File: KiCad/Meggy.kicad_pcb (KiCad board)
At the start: 4 copper layers, 17.4 x 54 mm, 24 parts, among them J1 USB_B_Micro, J2 Conn_01x03, Q1 DMP2305U-7, Q2 DMP2305U-7, Q3 DMP2305U-7, U1 ROM-socket-42pin, U2 AT90USB1286-MU, U3 M29F160F, X1 Standard_Clock_Oscillators_XT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

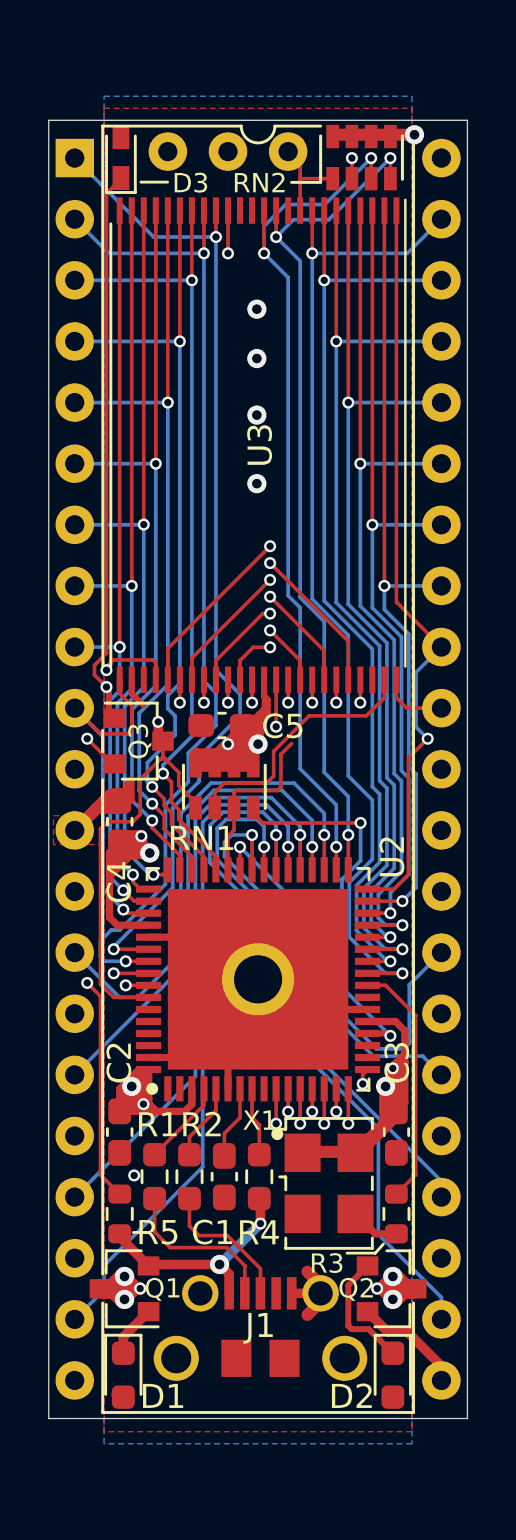
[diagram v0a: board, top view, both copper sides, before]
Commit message: Add push button for RESET and HWB lines
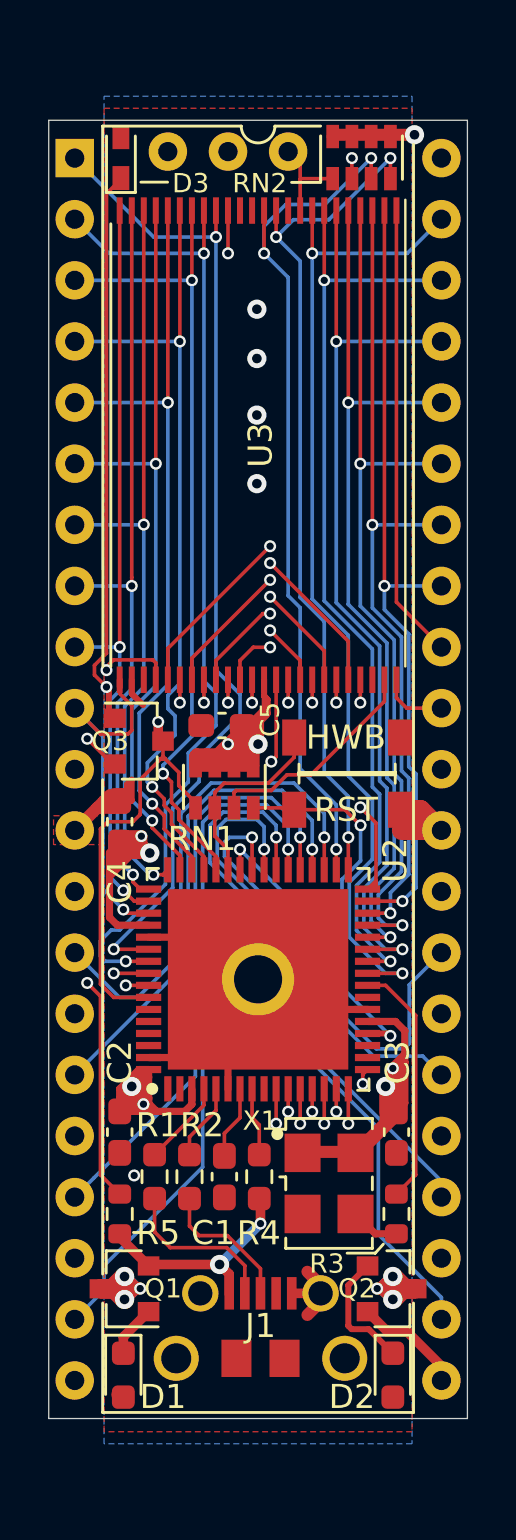
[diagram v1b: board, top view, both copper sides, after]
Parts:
- added SW1: SW_Push, Meggy:Sunrom_Tactile_Switch_3x4x2mm_SMD_2-Pin, F.Cu at (135.7, 86.0)
- added SW2: SW_Push, Meggy:Sunrom_Tactile_Switch_3x4x2mm_SMD_2-Pin, F.Cu at (135.7, 83.0)
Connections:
- RN1 pad 2: BYTE -> HWB
- RN1 pad 3: HWB -> BYTE
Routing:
- net GND: track 32.3 -> 38.1 mm
- net BYTE: track 10.7 -> 9.36 mm
- net HWB: track 7.35 -> 8.17 mm
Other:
- board text added: "HWB"
- board text added: "RST"

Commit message: Add 3D model for push buttons and fix names on pads not used (NC)
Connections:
- net AREF renamed /AREF_(NC)
- net NC renamed /A19_(NC)
- net PE3 renamed /PE3_(NC)
- net PE4 renamed /PE4_(NC)
- net PE5 renamed /PE5_(NC)
- net PE6 renamed /PE6_(NC)
- net PE7 renamed /PE7_(NC)
- net PF0 renamed /PF0_(NC)
- net PF1 renamed /PF1_(NC)
- net PF2 renamed /PF2_(NC)
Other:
- board text added: "B"
- board text added: "R"

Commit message: Moving into 6-layer PCB design
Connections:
- net XTAL2 renamed /XTAL2_(NC)
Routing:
- net BOARD_5V: track 96.6 -> 97.6 mm
- net A16: track 24.9 -> 24.0 mm
- added copper zone on 5V_BOARD, net BOARD_5V
- added copper zone on GND2, net GND
- added copper zone on Inner_signal.Cu, net VCC
- removed copper zone on VCC, net VCC
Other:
- copper layers 4 -> 6

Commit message: Re-routing improvements inner signal layer
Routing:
- net BOARD_5V: track 97.6 -> 96.7 mm

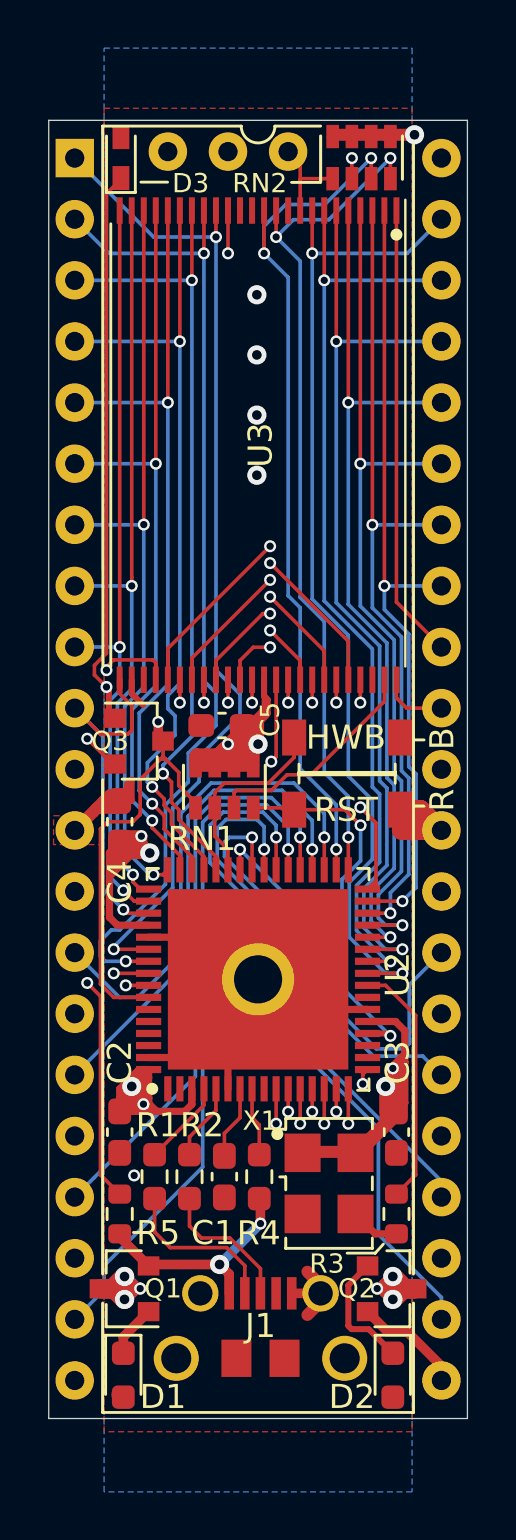
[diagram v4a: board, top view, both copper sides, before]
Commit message: Re-routing improvements underside signal layer
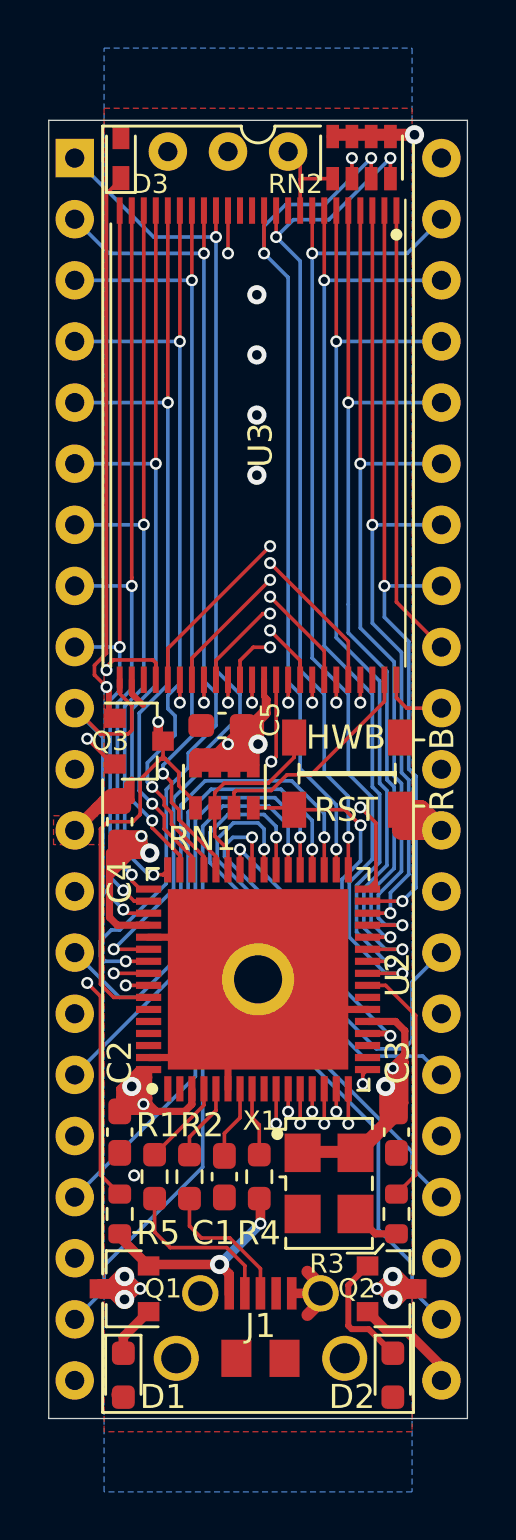
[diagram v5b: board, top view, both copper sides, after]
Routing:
- net BOARD_5V: track 96.7 -> 100.6 mm

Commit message: Re-routing improvements top side signal layer
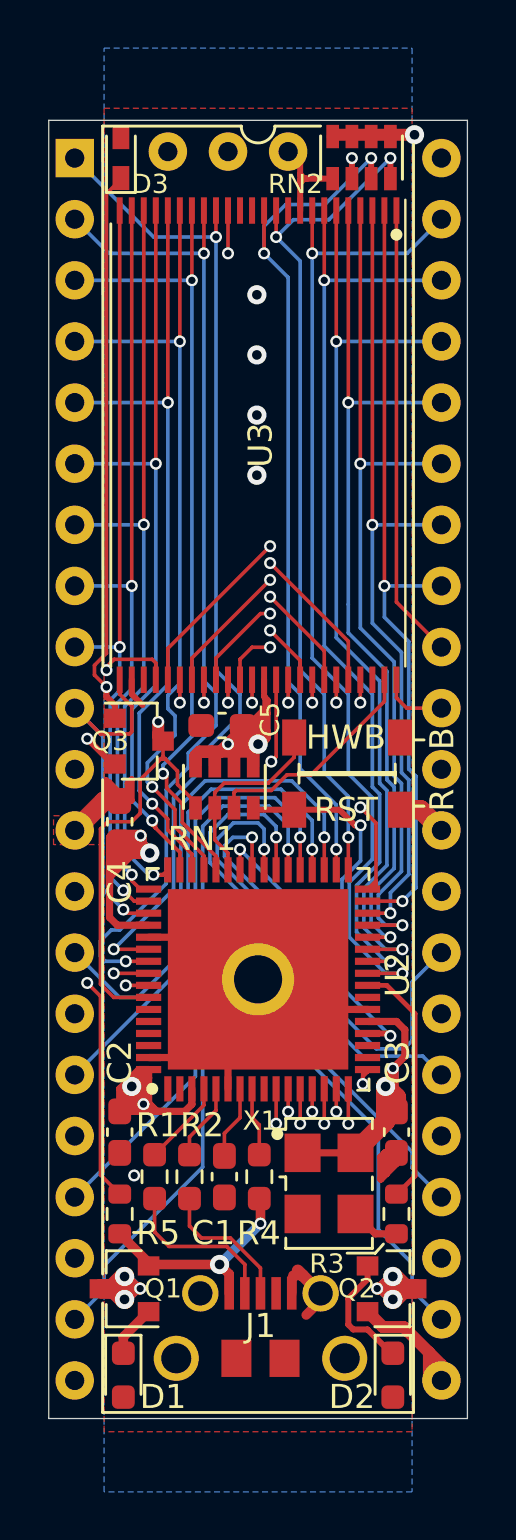
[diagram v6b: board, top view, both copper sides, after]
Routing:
- net BOARD_5V: track 100.6 -> 90.1 mm
- net GND: track 38.1 -> 41.0 mm
- net VCC: track 4.61 -> 6.33 mm
- net D15: track 21.4 -> 22.5 mm
- net OE_FLASH: track 24.5 -> 23.9 mm
- net A19: track 4.02 -> 4.63 mm

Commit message: Add keep out copper pour area for USB pin 4
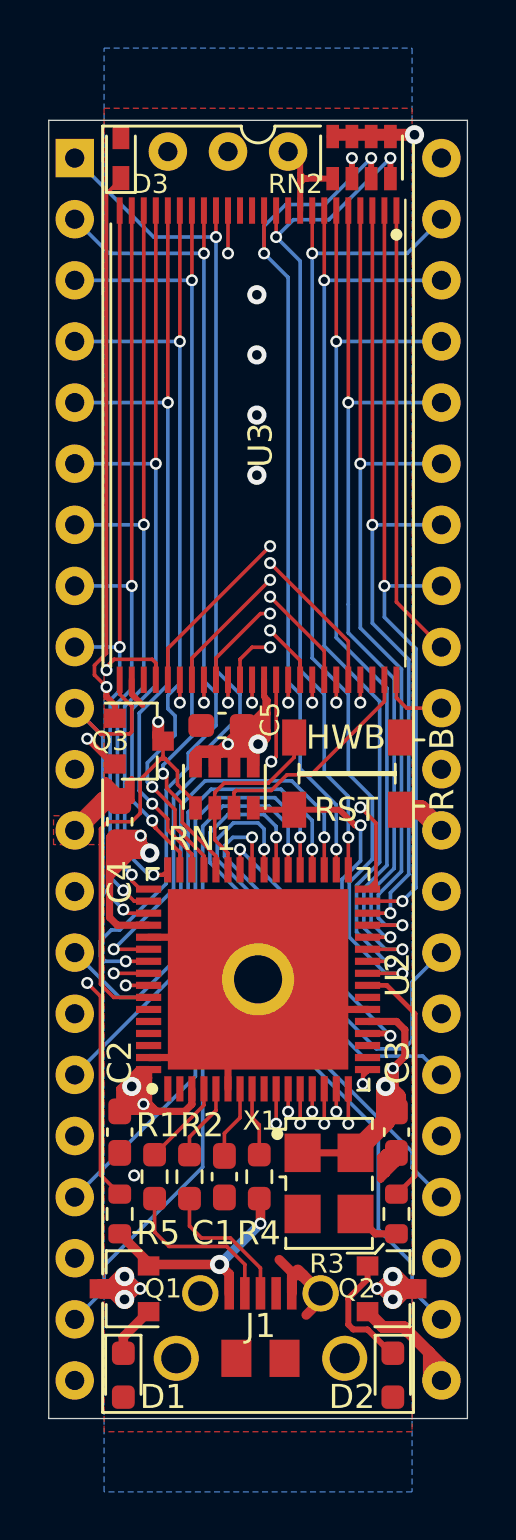
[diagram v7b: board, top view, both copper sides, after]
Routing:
- net GND: track 41.0 -> 42.6 mm

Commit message: Add silkscreen text and OSHW-symbol
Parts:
- added REF**: OSHW-Logo2_14.6x12mm_SilkScreen, Symbol:OSHW-Logo2_14.6x12mm_SilkScreen, B.Cu at (131.7, 99.3)
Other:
- board text added: "1MB KS ROM switch for A500+"
- board text added: "Meggy"
- board text added: "Rev. A Design by J.Bilander (C) 2025"
